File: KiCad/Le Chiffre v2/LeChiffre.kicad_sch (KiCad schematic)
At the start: 93 parts, among them J1 Conn_01x03_Female, J2 Conn_01x04_Female, SW1 SW_Push, SW10 SW_Push, SW11 SW_Push, SW12 SW_Push, SW13 SW_Push, SW14 SW_Push, SW15 SW_Push, SW16 SW_Push, SW17 SW_Push, SW18 SW_Push, SW19 SW_Push, SW2 SW_Push, SW20 SW_Push, SW21 SW_Push, SW22 SW_Push, SW23 SW_Push, SW24 SW_Push, SW25 SW_Push, SW26 SW_Push, SW27 SW_Push, SW28 SW_Push, SW29 SW_Push, SW3 SW_Push, SW30 SW_Push, SW31 SW_Push, SW32 SW_Push, SW33 SW_Push, SW34 SW_Push, SW35 SW_Push, SW36 Rotary_Encoder_Switch, SW37 SW_Push, SW38 SW_Push, SW39 SW_Push, SW4 SW_Push, SW5 SW_Push, SW6 SW_Push, SW7 SW_Push, SW8 SW_Push, SW9 SW_Push, U1 elite-nano-combo-controller, U2 SN74HC595

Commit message: rainbow mode
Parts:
- removed D101, D102, D103, D104, D105, D106, D107, D108, D109, D110, D111: WS2812B, LED_SMD:LED_WS2812B_PLCC4_5.0x5.0mm_P3.2mm, symbol LED:WS2812B
- removed J1: Conn_01x03_Female, Connector_PinSocket_2.54mm:PinSocket_1x03_P2.54mm_Vertical, symbol LeChiffre-rescue:Conn_01x03_Female-Connector
- added D38, D39, D40, D41, D42, D43, D44, D45, D46, D47, D48, D49, D50, D51, D52, D53, D54, D55, D56, D57, D58, D59, D60, D61, D62, D63, D64, D65, D66, D67, D68, D69, D70, D71, D72, D73, D74, D75, D76, D77, D78, D79, D80, D81, D82, D83, D84: SK6803_MINI-E, dek:SK6803-MINI-E, symbol dek:SK6803_MINI-E
- added JP1: SolderJumper_3_Open, Jumper:SolderJumper-3_P1.3mm_Open_RoundedPad1.0x1.5mm, symbol Jumper:SolderJumper_3_Open
- added Q1: AO3401A, Package_TO_SOT_SMD:SOT-23_Handsoldering, symbol Transistor_FET:AO3401A
- added Q2: AO3400A, Package_TO_SOT_SMD:SOT-23_Handsoldering, symbol Transistor_FET:AO3400A
- added R1, R4: 100K, Resistor_SMD:R_0805_2012Metric_Pad1.20x1.40mm_HandSolder, symbol Device:R
- added R2, R3: 1K, Resistor_SMD:R_0805_2012Metric_Pad1.20x1.40mm_HandSolder, symbol Device:R
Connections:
- net EncA: now also SW36.B; no longer SW36.A
- net EncB: now also SW36.A; no longer SW36.B
- net GND: now also D38.3 (VSS), D39.3 (VSS), D40.3 (VSS), D41.3 (VSS), D42.3 (VSS), D43.3 (VSS), D44.3 (VSS), D45.3 (VSS), D46.3 (VSS), D47.3 (VSS), D48.3 (VSS), D49.3 (VSS), D50.3 (VSS), D51.3 (VSS), D52.3 (VSS), D53.3 (VSS), D54.3 (VSS), D55.3 (VSS), D56.3 (VSS), D57.3 (VSS), D58.3 (VSS), D59.3 (VSS), D60.3 (VSS), D61.3 (VSS), D62.3 (VSS), D63.3 (VSS), D64.3 (VSS), D65.3 (VSS), D66.3 (VSS), D67.3 (VSS), D68.3 (VSS), D69.3 (VSS), D70.3 (VSS), D71.3 (VSS), D72.3 (VSS), D73.3 (VSS), D74.3 (VSS), D75.3 (VSS), D76.3 (VSS), D77.3 (VSS), D78.3 (VSS), D79.3 (VSS), D80.3 (VSS), D81.3 (VSS), D82.3 (VSS), D83.3 (VSS), D84.3 (VSS), Q2.2 (S), R4.1
- net RAW: now also JP1.1 (A)
- net VCC: now also JP1.3 (B)
- net LED_PWR_SW: now reaches U1.12 (9/PB5)
- net LED_PWR_SW: now also R3.1, R4.2
- net LED renamed LED_DATA
- net LED_DATA: now also D38.4 (DIN)
- new net: D39.2 (DOUT), D40.4 (DIN)
- new net: D38.2 (DOUT), D39.4 (DIN)
- new net: D46.2 (DOUT), D54.4 (DIN)
- new net: D46.4 (DIN), D47.2 (DOUT)
- new net: D58.2 (DOUT), D59.4 (DIN)
- new net: D57.2 (DOUT), D58.4 (DIN)
- new net: D43.2 (DOUT), D44.4 (DIN)
- new net: D42.2 (DOUT), D43.4 (DIN)
- new net: D78.4 (DIN), D79.2 (DOUT)
- new net: D79.4 (DIN), D80.2 (DOUT)
- new net: D61.2 (DOUT), D69.4 (DIN)
- new net: D60.2 (DOUT), D61.4 (DIN)
- new net: D48.4 (DIN), D49.2 (DOUT)
- new net: D49.4 (DIN), D50.2 (DOUT)
- new net: D64.4 (DIN), D65.2 (DOUT)
- new net: D65.4 (DIN), D66.2 (DOUT)
- new net: D80.4 (DIN), D81.2 (DOUT)
- new net: D70.2 (DOUT), D71.4 (DIN)
- new net: D62.2 (DOUT), D70.4 (DIN)
- new net: D47.4 (DIN), D48.2 (DOUT)
- new net: D71.2 (DOUT), D72.4 (DIN)
- new net: D41.2 (DOUT), D42.4 (DIN)
- new net: D40.2 (DOUT), D41.4 (DIN)
- new net: D56.2 (DOUT), D57.4 (DIN)
- new net: D44.2 (DOUT), D45.4 (DIN)
- new net: D83.4 (DIN), D84.2 (DOUT)
- new net: D77.2 (DOUT), D84.4 (DIN)
- new net: D52.4 (DIN), D53.2 (DOUT)
- new net: D45.2 (DOUT), D53.4 (DIN)
- new net: D76.2 (DOUT), D77.4 (DIN)
- new net: D75.2 (DOUT), D76.4 (DIN)
- new net: D62.4 (DIN), D63.2 (DOUT)
- new net: D63.4 (DIN), D64.2 (DOUT)
- new net: D55.2 (DOUT), D56.4 (DIN)
- new net: D54.2 (DOUT), D55.4 (DIN)
- new net: D50.4 (DIN), D51.2 (DOUT)
- new net: D51.4 (DIN), D52.2 (DOUT)
- new net: D82.4 (DIN), D83.2 (DOUT)
- new net: D81.4 (DIN), D82.2 (DOUT)
- new net: D66.4 (DIN), D67.2 (DOUT)
- new net: D74.2 (DOUT), D75.4 (DIN)
- new net: D73.2 (DOUT), D74.4 (DIN)
- new net: Q1.1 (G), R2.2
- new net: Q2.3 (D), R1.2, R2.1
- new net: D59.2 (DOUT), D60.4 (DIN)
- new net: D72.2 (DOUT), D73.4 (DIN)
- new net: Q2.1 (G), R3.2
- new net: D68.4 (DIN), D69.2 (DOUT)
- new net: D67.4 (DIN), D68.2 (DOUT)
- new net LED_PWR_IN: JP1.2 (C), Q1.2 (S), R1.1
- new net LED_PWR_OUT: D38.1 (VDD), D39.1 (VDD), D40.1 (VDD), D41.1 (VDD), D42.1 (VDD), D43.1 (VDD), D44.1 (VDD), D45.1 (VDD), D46.1 (VDD), D47.1 (VDD), D48.1 (VDD), D49.1 (VDD), D50.1 (VDD), D51.1 (VDD), D52.1 (VDD), D53.1 (VDD), D54.1 (VDD), D55.1 (VDD), D56.1 (VDD), D57.1 (VDD), D58.1 (VDD), D59.1 (VDD), D60.1 (VDD), D61.1 (VDD), D62.1 (VDD), D63.1 (VDD), D64.1 (VDD), D65.1 (VDD), D66.1 (VDD), D67.1 (VDD), D68.1 (VDD), D69.1 (VDD), D70.1 (VDD), D71.1 (VDD), D72.1 (VDD), D73.1 (VDD), D74.1 (VDD), D75.1 (VDD), D76.1 (VDD), D77.1 (VDD), D78.1 (VDD), D79.1 (VDD), D80.1 (VDD), D81.1 (VDD), D82.1 (VDD), D83.1 (VDD), D84.1 (VDD), Q1.3 (D)
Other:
- moved on the sheet: D1, D10, D11, D12, D13, D14, D15, D16, D17, D18, D19, D2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

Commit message: Added PCBA for Dasky's changes
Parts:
- D38, D39, D40, D41, D42, D43, D44, D45, D46, D47, D48, D49, D50, D51, D52, D53, D54, D55, D56, D57, D58, D59, D60, D61, D62, D63, D64, D65, D66, D67, D68, D69, D70, D71, D72, D73, D74, D75, D76, D77, D78, D79, D80, D81, D82, D83, D84: LCSC (none) -> C5242955
- Q1: LCSC (none) -> C306862
- Q2: LCSC (none) -> C332101
- R1, R4: LCSC (none) -> C416061
- R2, R3: LCSC (none) -> C416075

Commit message: added vik support, and extra spi through holes
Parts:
- removed Q1: AO3401A, Package_TO_SOT_SMD:SOT-23_Handsoldering, symbol Transistor_FET:AO3401A
- removed Q2: AO3400A, Package_TO_SOT_SMD:SOT-23_Handsoldering, symbol Transistor_FET:AO3400A
- removed R1, R4: 100K, Resistor_SMD:R_0805_2012Metric_Pad1.20x1.40mm_HandSolder, symbol Device:R
- removed R2, R3: 1K, Resistor_SMD:R_0805_2012Metric_Pad1.20x1.40mm_HandSolder, symbol Device:R
- added J1: Conn_01x06_Socket, Connector_PinHeader_2.54mm:PinHeader_1x06_P2.54mm_Vertical, symbol Connector:Conn_01x06_Socket
- added J3: ~, vik:vik-keyboard-connector-horizontal, symbol vik:vik-keyboard-connector
- added JP2: Jumper_3_Bridged12, Jumper:SolderJumper-3_P1.3mm_Bridged12_RoundedPad1.0x1.5mm, symbol Jumper:Jumper_3_Bridged12
- U1: value elite-nano-combo-controller -> pro-micro-controller; footprint dek:elite-nano-combo-controller -> dek:pro-micro-controller; symbol dek:elite-nano-combo-controller -> dek:pro-micro-controller
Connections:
- net LED_PWR_IN is gone; now on net LED_PWR_OUT: JP1.2 (C)
- net LED_PWR_SW is gone; now on net row4: U1.12 (9/PB5)
- net GND: now also J1.1 (Pin_1), J3.2 (GND)
- net LED_DATA: now also JP2.2 (C); no longer D38.4 (DIN)
- net MOSI: now also J1.2 (Pin_2), J3.8 (MOSI)
- net RAW: now also J3.6 (5V)
- net SCL: now also J3.4 (SCL)
- net SCLK: now also J1.5 (Pin_5), J3.12 (SCLK)
- net SDA: now also J3.3 (SDA)
- net VCC: now also J1.6 (Pin_6), J3.1 (3V3)
- net row0: now also U1.8 (5/PC6); no longer U1.19 (A2/PF5)
- net row1: now also U1.9 (6/PD7); no longer U1.17 (A0/PF7)
- net row2: now also U1.10 (7/PE6); no longer U1.18 (A1/PF6)
- net row3: now also U1.11 (8/PB4); no longer U1.20 (A3/PF4)
- net row4: no longer U1.8 (5/PC6)
- net VIK_RGB_DATA: now reaches D78.2 (DOUT)
- net VIK_RGB_DATA: now also J3.5 (RGB_DO), JP2.3 (B)
- net MISO: now reaches U1.15 (14/PB3)
- net MISO: now also J1.4 (Pin_4), J3.11 (MISO)
- new net: D38.4 (DIN), JP2.1 (A)
- new net GPIO_AD_1: J3.7 (GP_AD1), U1.19 (A2/PF5)
- new net GPIO_AD_2: J3.9 (GP_AD2), U1.20 (A3/PF4)
- new net SPI_CS: J1.3 (Pin_3), J3.10 (SPI_CS), U1.17 (A0/PF7)
- no-connect marks 10 -> 1
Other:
- note added: "SPI through hole"
- note added: "VIK"
- note removed: "Might want to reserve this one for MISO"

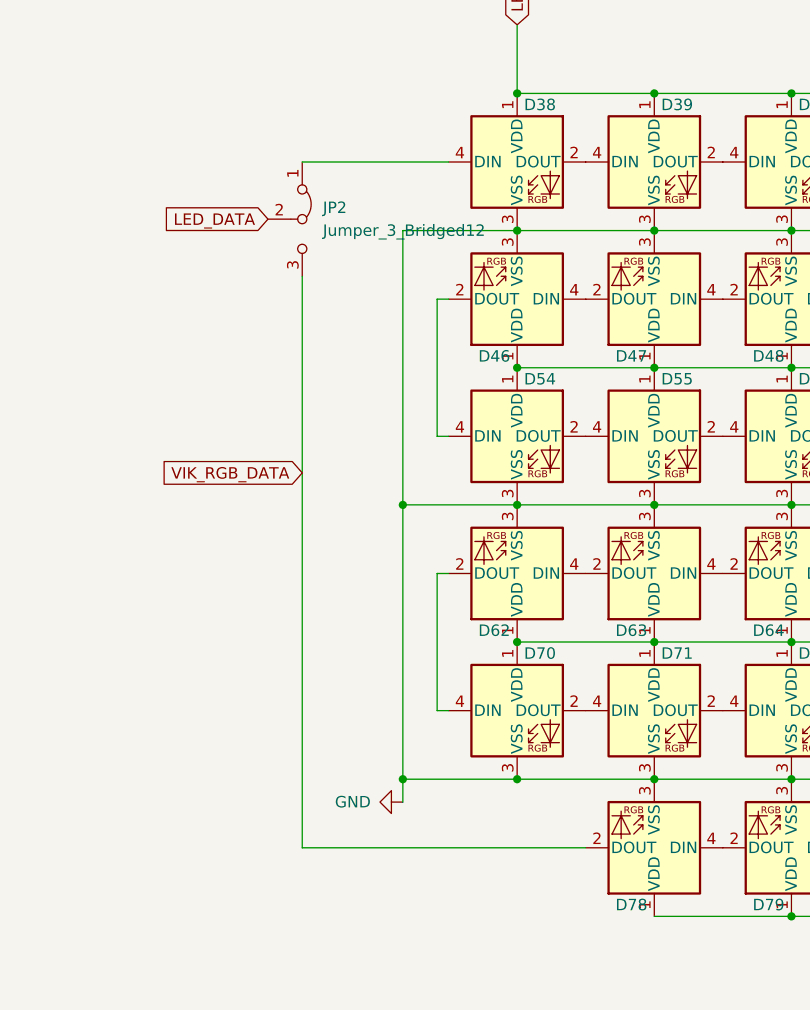
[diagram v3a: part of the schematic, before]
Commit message: led data no longer bridged by default, and fixed silk for vikification message
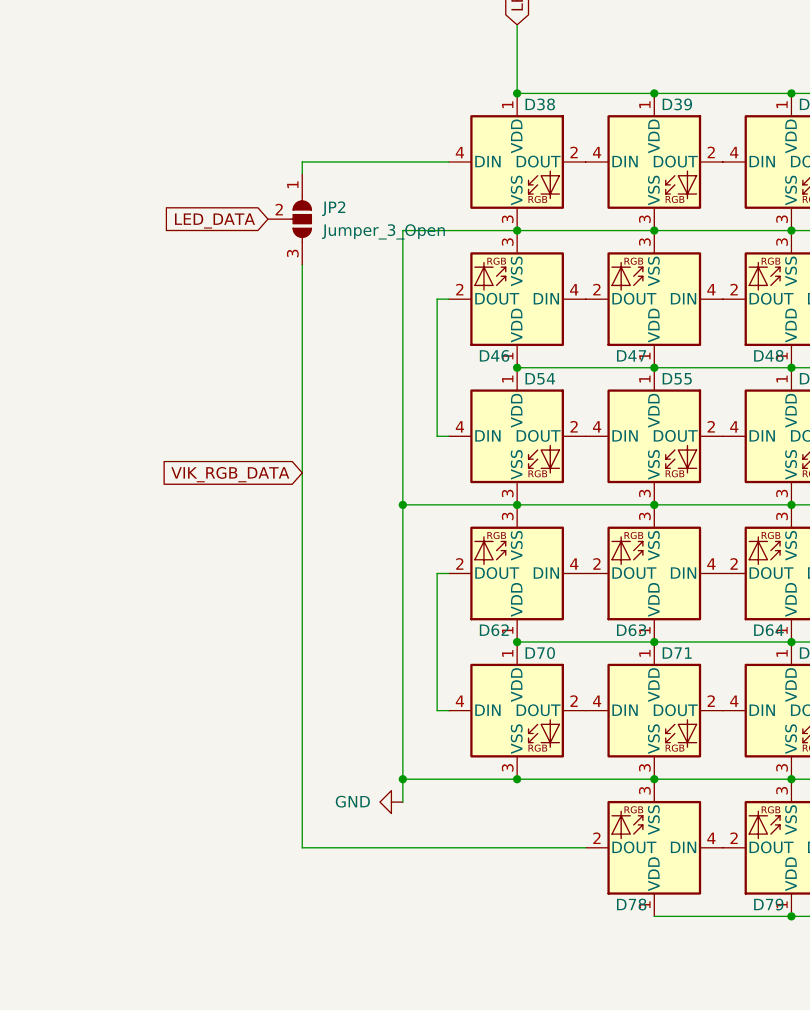
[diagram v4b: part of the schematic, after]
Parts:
- JP2: value Jumper_3_Bridged12 -> Jumper_3_Open; footprint Jumper:SolderJumper-3_P1.3mm_Bridged12_RoundedPad1.0x1.5mm -> Jumper:SolderJumper-3_P1.3mm_Open_RoundedPad1.0x1.5mm; symbol Jumper:Jumper_3_Bridged12 -> Jumper:SolderJumper_3_Open
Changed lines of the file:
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@@
     (stroke (width 0) (type default))
   )
-  (wire (pts (xy 259.334 240.03) (xy 259.334 176.53))
+  (wire (pts (xy 259.334 175.26) (xy 259.334 240.03))
     (stroke (width 0) (type default))
   )
@@
     (stroke (width 0) (type default))
   )
+  (wire (pts (xy 259.334 163.83) (xy 259.334 165.1))
+    (stroke (width 0) (type default))
+  )
   (wire (pts (xy 68.58 189.23) (xy 82.55 189.23))
     (stroke (width 0) (type default))
@@
     )
   )
-  (symbol (lib_id "Jumper:Jumper_3_Bridged12") (at 259.334 170.18 270) (unit 1)
+  (symbol (lib_id "Jumper:SolderJumper_3_Open") (at 259.334 170.18 270) (unit 1)
     (in_bom yes) (on_board yes) (dnp no) (fields_autoplaced)
     (property "Reference" "JP2" (at 261.62 168.91 90)
       (effects (font (size 1.27 1.27)) (justify left))
     )
-    (property "Value" "Jumper_3_Bridged12" (at 261.62 171.45 90)
+    (property "Value" "Jumper_3_Open" (at 261.62 171.45 90)
       (effects (font (size 1.27 1.27)) (justify left))
     )
-    (property "Footprint" "Jumper:SolderJumper-3_P1.3mm_Bridged12_RoundedPad1.0x1.5mm" (at 259.334 170.18 0)
+    (property "Footprint" "Jumper:SolderJumper-3_P1.3mm_Open_RoundedPad1.0x1.5mm" (at 259.334 170.18 0)
       (effects (font (size 1.27 1.27)) hide)
     )

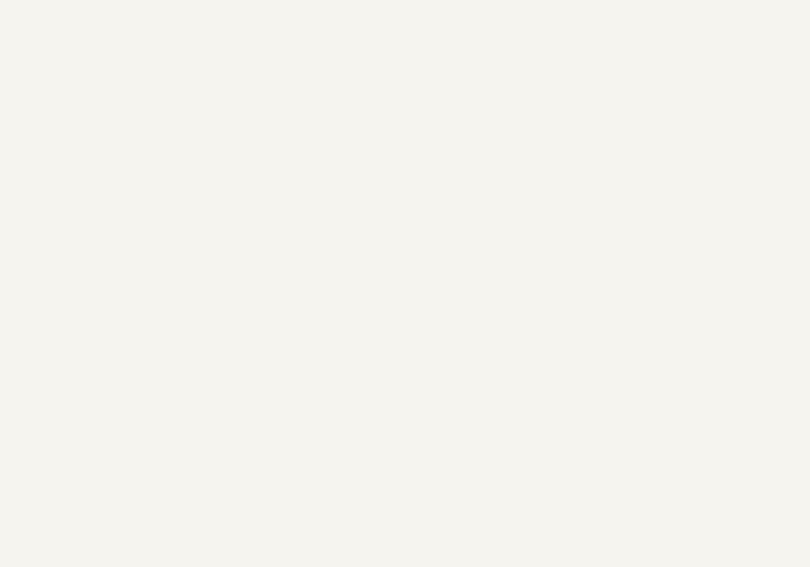
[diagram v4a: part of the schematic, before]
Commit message: added trackpoint mounting support
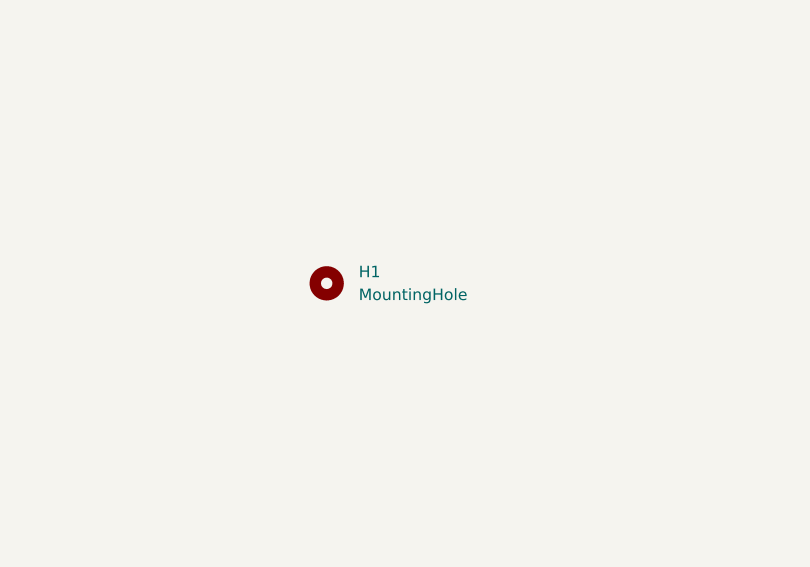
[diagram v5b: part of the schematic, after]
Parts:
- added H1: MountingHole, dek:TPSensorModule, symbol Mechanical:MountingHole
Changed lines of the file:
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@@
+    )
+  )
+  (symbol (lib_id "Mechanical:MountingHole") (at 255.524 66.04 0) (unit 1)
+    (in_bom yes) (on_board yes) (dnp no) (fields_autoplaced)
+    (property "Reference" "H1" (at 259.08 64.77 0)
+      (effects (font (size 1.27 1.27)) (justify left))
+    )
+    (property "Value" "MountingHole" (at 259.08 67.31 0)
+      (effects (font (size 1.27 1.27)) (justify left))
+    )
+    (property "Footprint" "dek:TPSensorModule" (at 255.524 66.04 0)
+      (effects (font (size 1.27 1.27)) hide)
+    )
+    (property "Datasheet" "~" (at 255.524 66.04 0)
+      (effects (font (size 1.27 1.27)) hide)
+    )
+    (instances
+      (project "LeChiffre"
+        (path "/5e5e707a-d2a3-4526-80ff-784131c01bf7"
+          (reference "H1") (unit 1)
+        )
+      )
     )
   )
